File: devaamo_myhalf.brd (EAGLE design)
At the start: 48 x 39 mm, 19 parts, among them X1 PIIKKIRIMA-10

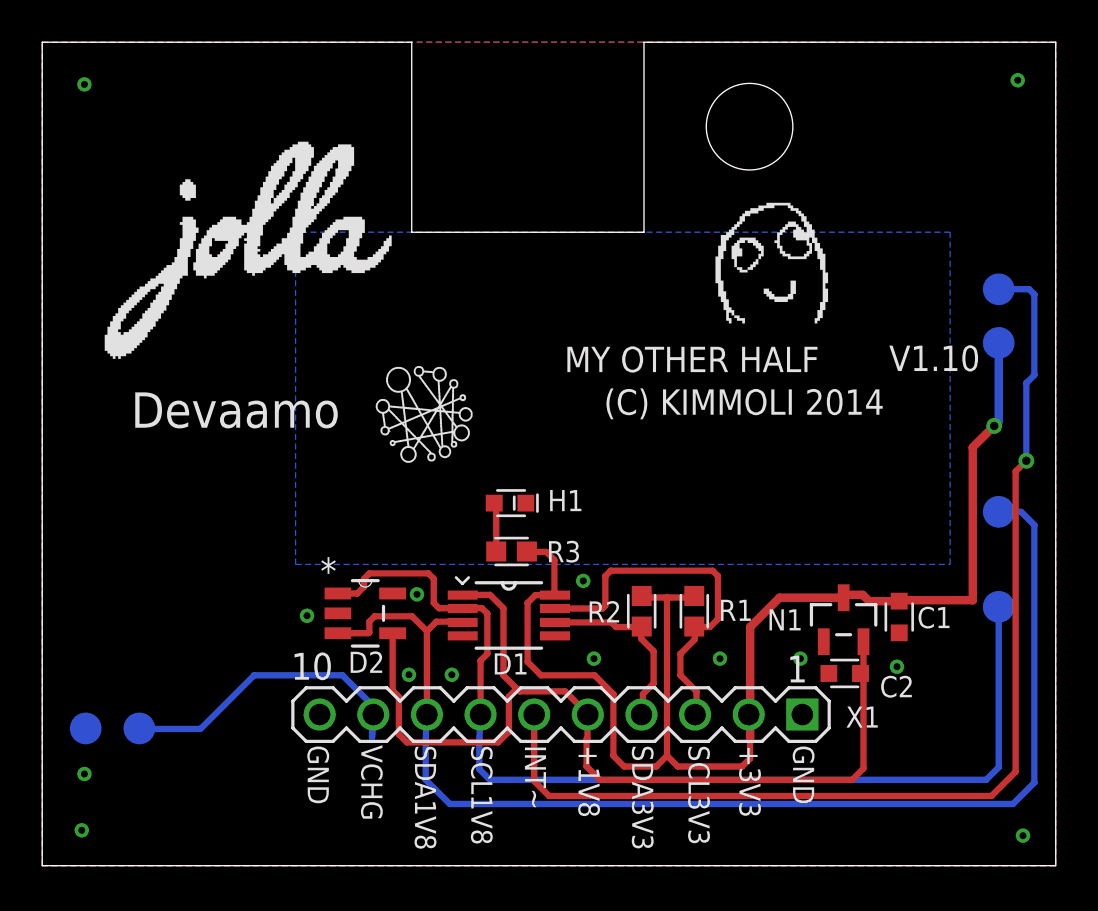
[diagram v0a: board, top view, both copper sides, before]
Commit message: smd connector add, relocate flash hole, resize pogopads to 2mm
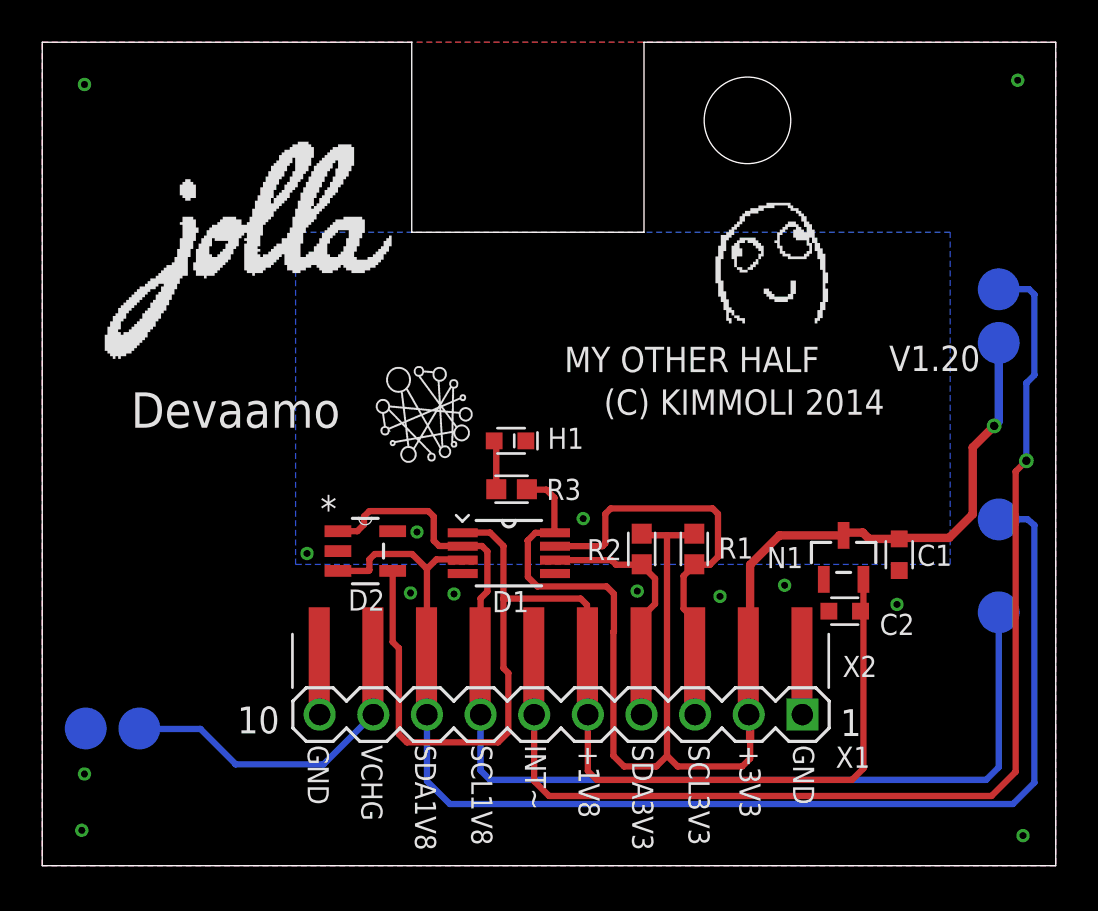
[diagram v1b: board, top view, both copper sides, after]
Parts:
- added X2: PIIKKIRIMA-10SMD-WIRE, OMAT_IC:61001018321
- X1: value PIIKKIRIMA-10 -> PIIKKIRIMA-10TH
- moved C2 2.95 mm to (38.0, 12.1)
- moved N1 2.95 mm to (38.0, 14.6)
- moved C1 2.95 mm to (40.6, 14.7)
- moved D1 2.95 mm to (22.1, 14.8)
- moved D2 2.95 mm to (15.3, 14.9)
- moved H1 2.95 mm to (22.2, 20.1)
- moved R1 2.95 mm to (30.9, 15.0)
- moved R2 2.95 mm to (28.4, 15.0)
- moved R3 2.95 mm to (22.2, 17.8)
- moved SDA 0.36 mm to (45.3, 16.4)
- moved SCL 0.26 mm to (45.3, 12.0)
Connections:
- net +1V8: now also X2.6
- net +3V3: now also X2.9
- net GND: now also X2.1, X2.10
- net INT: now also X2.5
- net SCL_1V8: now also X2.4
- net SCL_3V3: now also X2.8
- net SDA_1V8: now also X2.3
- net SDA_3V3: now also X2.7
- net VCC: now also X2.2
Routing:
- net +1V8: track 45.1 -> 59.1 mm
- net +3V3: track 63.8 -> 72.1 mm
- net SDA_1V8: track 57.9 -> 63.3 mm
- net SCL_1V8: track 49.3 -> 54.5 mm
- net SDA_3V3: track 8.84 -> 11.9 mm
- net SCL_3V3: track 17.5 -> 20.2 mm
- net INT: track 51.5 -> 54.0 mm
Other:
- board text added: "V1.20"
- board text removed: "V1.10"

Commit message: oshw logo added
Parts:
- added LOGO1: OSHW_LOGO_FILLX0200-NT, ohw-logo:OSHW_FILLX200_NOTEXT
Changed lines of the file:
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@@
 <attribute name="VALUE" x="9.062" y="2.4958" size="1.27" layer="27"/>
 </element>
+<element name="LOGO1" library="ohw-logo" package="OSHW_FILLX200_NOTEXT" value="OSHW_LOGO_FILLX0200-NT" x="3.425" y="8.675"/>
 </elements>
 <signals>
